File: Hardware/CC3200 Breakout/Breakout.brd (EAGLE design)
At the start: 58.4 x 76.3 mm, 5 parts, among them P1 SSW-110-02-G-D, P2 SSW-110-02-G-D, X1 TSW-105-07-G-S

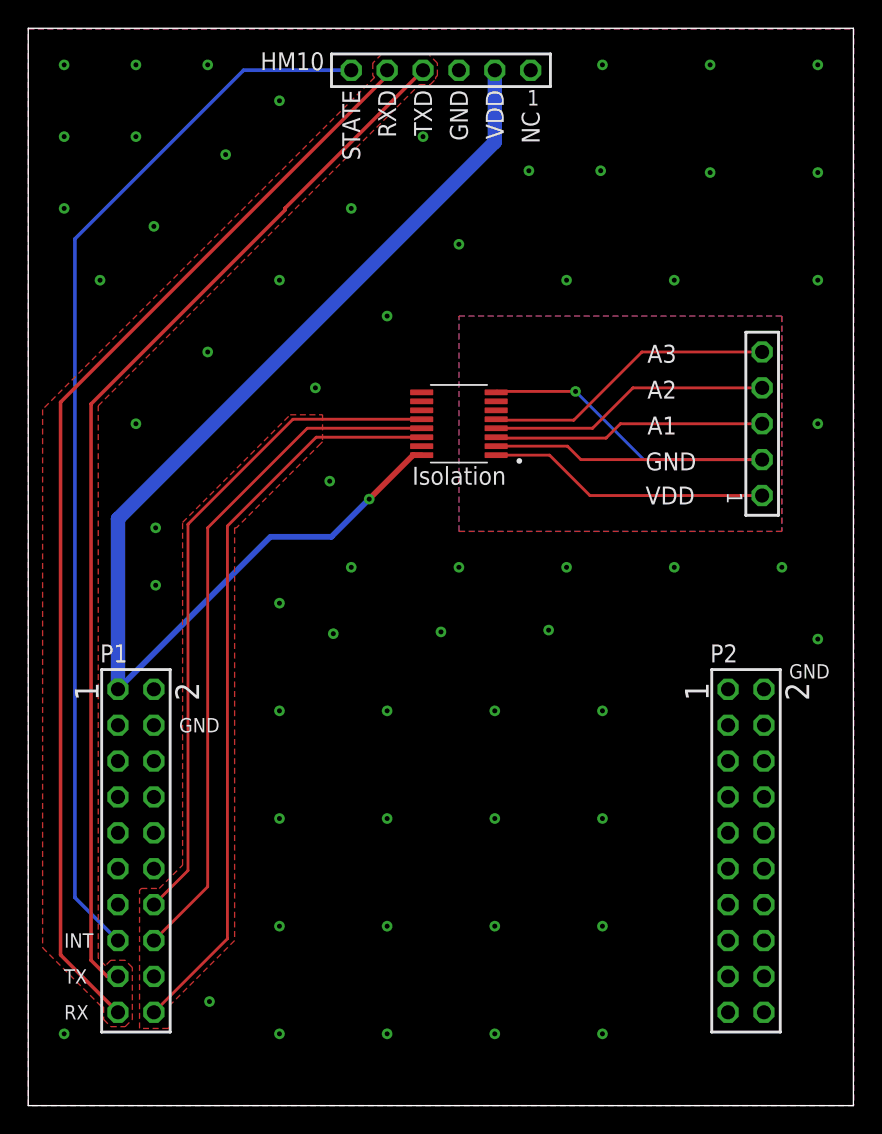
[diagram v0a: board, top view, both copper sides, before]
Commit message: Updated the breakout schematics
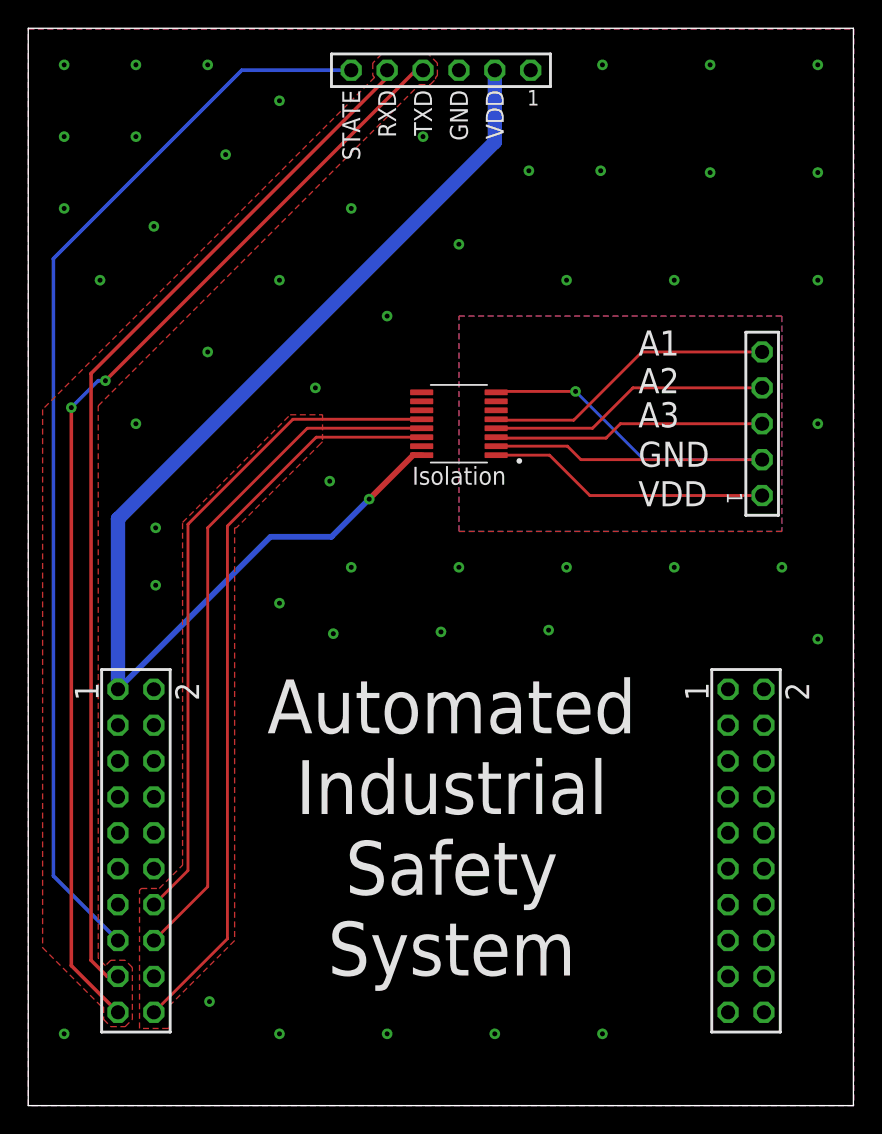
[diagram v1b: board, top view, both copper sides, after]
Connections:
- removed net RX: HM10.5, P1.19
- removed net TX: HM10.4, P1.17
- new net 3200_RX: HM10.4, P1.19
- new net 3200_TX: HM10.5, P1.17
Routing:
- net 3200_RX: track 0.00 -> 78.9 mm, vias 0 -> 2
- net RX: track 77.9 -> 0.00 mm
- net TX: track 75.1 -> 0.00 mm
- net 3200_TX: track 0.00 -> 74.1 mm
- net STATE: track 75.4 -> 76.8 mm
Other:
- board text added: "Automated Industrial Safety System"
- board text removed: "INT"
- board text removed: "NC"
- board text removed: "RX"
- board text removed: "TX"
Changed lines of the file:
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@@
 <layer number="24" name="bOrigins" color="15" fill="1" visible="yes" active="yes"/>
 <layer number="25" name="tNames" color="7" fill="1" visible="yes" active="yes"/>
-<layer number="26" name="bNames" color="7" fill="1" visible="yes" active="yes"/>
-<layer number="27" name="tValues" color="7" fill="1" visible="yes" active="yes"/>
-<layer number="28" name="bValues" color="7" fill="1" visible="yes" active="yes"/>
+<layer number="26" name="bNames" color="7" fill="1" visible="no" active="yes"/>
+<layer number="27" name="tValues" color="7" fill="1" visible="no" active="yes"/>
+<layer number="28" name="bValues" color="7" fill="1" visible="no" active="yes"/>
 <layer number="29" name="tStop" color="7" fill="3" visible="no" active="yes"/>
 <layer number="30" name="bStop" color="7" fill="6" visible="no" active="yes"/>
@@
 <dimension x1="6.35" y1="6.604" x2="6.35" y2="0" x3="-10.16" y3="3.302" textsize="1.778" layer="47" unit="mil" precision="3"/>
 <dimension x1="35.56" y1="73.279" x2="35.56" y2="76.2" x3="63.5" y3="74.7395" textsize="1.778" layer="47" unit="mil" precision="3"/>
-<text x="2.54" y="6.096" size="1.016" layer="25">RX</text>
-<text x="2.54" y="8.636" size="1.016" layer="25">TX</text>
-<text x="2.54" y="11.176" size="1.016" layer="25">INT</text>
-<text x="10.668" y="26.416" size="1.016" layer="25">GND</text>
-<text x="32.385" y="71.882" size="1.27" layer="25" rot="R270">VDD</text>
-<text x="29.845" y="71.882" size="1.27" layer="25" rot="R270">GND</text>
-<text x="27.305" y="71.882" size="1.27" layer="25" rot="R270">TXD</text>
-<text x="24.765" y="71.882" size="1.27" layer="25" rot="R270">RXD</text>
-<text x="22.225" y="71.882" size="1.27" layer="25" rot="R270">STATE</text>
-<text x="34.925" y="70.358" size="1.27" layer="25" rot="R270">NC</text>
-<text x="43.688" y="42.545" size="1.27" layer="25">VDD</text>
-<text x="43.688" y="44.958" size="1.27" layer="25">GND</text>
-<text x="43.815" y="47.498" size="1.27" layer="25">A1</text>
-<text x="43.815" y="50.038" size="1.27" layer="25">A2</text>
-<text x="43.815" y="52.578" size="1.27" layer="25">A3</text>
-<text x="27.178" y="43.942" size="1.27" layer="25">Isolation</text>
-<text x="53.848" y="30.226" size="1.016" layer="25">GND</text>
+<text x="32.385" y="71.882" size="1.27" layer="21" rot="R270">VDD</text>
+<text x="29.845" y="71.882" size="1.27" layer="21" rot="R270">GND</text>
+<text x="27.305" y="71.882" size="1.27" layer="21" rot="R270">TXD</text>
+<text x="24.765" y="71.882" size="1.27" layer="21" rot="R270">RXD</text>
+<text x="22.225" y="71.882" size="1.27" layer="21" rot="R270">STATE</text>
+<text x="27.178" y="43.942" size="1.27" layer="21">Isolation</text>
+<text x="43.18" y="42.418" size="1.778" layer="21">VDD</text>
+<text x="43.18" y="45.212" size="1.778" layer="21">GND</text>
+<text x="43.18" y="48.006" size="1.778" layer="21">A3</text>
+<text x="43.18" y="50.419" size="1.778" layer="21">A2</text>
+<text x="43.18" y="53.086" size="1.778" layer="21">A1</text>
+<text x="29.972" y="19.685" size="3.81" layer="21" align="center">Automated
+Industrial
+Safety
+System</text>
 </plain>
 <attributes>
@@
 <attribute name="MF" value="Samtec Inc." x="52.07" y="35.179" size="1.778" layer="27" display="off"/>
 <attribute name="MPN" value="TSW-106-07-G-S" x="52.07" y="35.179" size="1.778" layer="27" display="off"/>
-<attribute name="NAME" x="20.955" y="74.549" size="1.27" layer="25" rot="R180"/>
 <attribute name="OC_FARNELL" value="" x="52.07" y="35.179" size="1.778" layer="27" display="off"/>
 <attribute name="OC_NEWARK" value="" x="52.07" y="35.179" size="1.778" layer="27" display="off"/>
@@
 <attribute name="MF" value="Samtec Inc." x="2.54" y="-9.906" size="1.778" layer="27" rot="R270" display="off"/>
 <attribute name="MPN" value="SSW-110-02-G-D" x="2.54" y="-9.906" size="1.778" layer="27" rot="R270" display="off"/>
-<attribute name="NAME" x="5.08" y="31.369" size="1.27" layer="25"/>
 <attribute name="OC_FARNELL" value="unknown" x="2.54" y="-9.906" size="1.778" layer="27" rot="R270" display="off"/>
 <attribute name="OC_NEWARK" value="11P9480" x="2.54" y="-9.906" size="1.778" layer="27" rot="R270" display="off"/>
@@
 <attribute name="MF" value="Samtec Inc." x="27.94" y="-9.906" size="1.778" layer="27" rot="R270" display="off"/>
 <attribute name="MPN" value="SSW-110-02-G-D" x="27.94" y="-9.906" size="1.778" layer="27" rot="R270" display="off"/>
-<attribute name="NAME" x="48.26" y="31.369" size="1.27" layer="25"/>
 <attribute name="OC_FARNELL" value="unknown" x="27.94" y="-9.906" size="1.778" layer="27" rot="R270" display="off"/>
 <attribute name="OC_NEWARK" value="11P9480" x="27.94" y="-9.906" size="1.778" layer="27" rot="R270" display="off"/>
@@
 <via x="22.86" y="38.1" extent="1-16" drill="0.35"/>
 <via x="17.78" y="35.56" extent="1-16" drill="0.35"/>
-<via x="17.78" y="27.94" extent="1-16" drill="0.35"/>
-<via x="17.78" y="20.32" extent="1-16" drill="0.35"/>
-<via x="17.78" y="12.7" extent="1-16" drill="0.35"/>
 <via x="12.827" y="7.366" extent="1-16" drill="0.35"/>
 <via x="2.54" y="5.08" extent="1-16" drill="0.35"/>
@@
 <via x="33.02" y="5.08" extent="1-16" drill="0.35"/>
 <via x="40.64" y="5.08" extent="1-16" drill="0.35"/>
-<via x="25.4" y="12.7" extent="1-16" drill="0.35"/>
-<via x="40.64" y="12.7" extent="1-16" drill="0.35"/>
-<via x="33.02" y="12.7" extent="1-16" drill="0.35"/>
-<via x="40.64" y="20.32" extent="1-16" drill="0.35"/>
-<via x="33.02" y="20.32" extent="1-16" drill="0.35"/>
-<via x="25.4" y="20.32" extent="1-16" drill="0.35"/>
-<via x="40.64" y="27.94" extent="1-16" drill="0.35"/>
-<via x="33.02" y="27.94" extent="1-16" drill="0.35"/>
-<via x="25.4" y="27.94" extent="1-16" drill="0.35"/>
 <via x="36.83" y="33.655" extent="1-16" drill="0.35"/>
 <via x="29.21" y="33.528" extent="1-16" drill="0.35"/>
@@
 <via x="55.88" y="66.04" extent="1-16" drill="0.35"/>
 </signal>
-<signal name="TX">
-<contactref element="HM10" pad="4"/>
-<contactref element="P1" pad="17"/>
-<wire x1="6.35" y1="9.144" x2="5.588" y2="9.144" width="0.254" layer="1"/>
-<wire x1="5.588" y1="9.144" x2="4.445" y2="10.287" width="0.254" layer="1"/>
-<wire x1="4.445" y1="10.287" x2="4.445" y2="49.657" width="0.254" layer="1"/>
-<wire x1="18.161" y1="63.5" x2="18.161" y2="63.373" width="0.254" layer="1"/>
-<wire x1="18.161" y1="63.5" x2="27.94" y2="73.279" width="0.254" layer="1"/>
-<wire x1="4.445" y1="49.657" x2="18.161" y2="63.373" width="0.254" layer="1"/>
-</signal>
-<signal name="RX">
-<contactref element="HM10" pad="5"/>
-<contactref element="P1" pad="19"/>
-<wire x1="25.4" y1="73.279" x2="25.4" y2="72.898" width="0.254" layer="1"/>
-<wire x1="25.4" y1="72.898" x2="2.286" y2="49.784" width="0.254" layer="1"/>
-<wire x1="2.286" y1="49.784" x2="2.286" y2="10.668" width="0.254" layer="1"/>
-<wire x1="2.286" y1="10.668" x2="6.35" y2="6.604" width="0.254" layer="1"/>
-</signal>
 <signal name="STATE">
 <contactref element="HM10" pad="6"/>
 <contactref element="P1" pad="15"/>
-<wire x1="6.35" y1="11.684" x2="3.302" y2="14.732" width="0.254" layer="16"/>
-<wire x1="3.302" y1="14.732" x2="3.302" y2="61.341" width="0.254" layer="16"/>
-<wire x1="22.86" y1="73.279" x2="15.24" y2="73.279" width="0.254" layer="16"/>
-<wire x1="15.24" y1="73.279" x2="3.302" y2="61.341" width="0.254" layer="16"/>
+<wire x1="6.35" y1="11.684" x2="1.778" y2="16.256" width="0.254" layer="16"/>
+<wire x1="1.778" y1="16.256" x2="1.778" y2="59.944" width="0.254" layer="16"/>
+<wire x1="22.86" y1="73.279" x2="15.113" y2="73.279" width="0.254" layer="16"/>
+<wire x1="15.113" y1="73.279" x2="1.778" y2="59.944" width="0.254" layer="16"/>
 </signal>
 <signal name="VBUS">
@@
 </polygon>
 </signal>
+<signal name="3200_RX">
+<contactref element="HM10" pad="4"/>
+<contactref element="P1" pad="19"/>
+<wire x1="6.35" y1="6.604" x2="3.048" y2="9.906" width="0.254" layer="1"/>
+<via x="3.048" y="49.403" extent="1-16" drill="0.35"/>
+<wire x1="3.048" y1="9.906" x2="3.048" y2="49.403" width="0.254" layer="1"/>
+<wire x1="3.048" y1="49.403" x2="4.953" y2="51.308" width="0.254" layer="16"/>
+<wire x1="4.953" y1="51.308" x2="5.461" y2="51.308" width="0.254" layer="16"/>
+<via x="5.461" y="51.308" extent="1-16" drill="0.35"/>
+<wire x1="5.461" y1="51.308" x2="27.432" y2="73.279" width="0.254" layer="1"/>
+<wire x1="27.432" y1="73.279" x2="27.94" y2="73.279" width="0.254" layer="1"/>
+</signal>
+<signal name="3200_TX">
+<contactref element="HM10" pad="5"/>
+<contactref element="P1" pad="17"/>
+<wire x1="6.35" y1="9.144" x2="5.588" y2="9.144" width="0.254" layer="1"/>
+<wire x1="5.588" y1="9.144" x2="4.445" y2="10.287" width="0.254" layer="1"/>
+<wire x1="25.4" y1="72.771" x2="25.4" y2="73.279" width="0.254" layer="1"/>
+<wire x1="4.445" y1="10.287" x2="4.445" y2="51.816" width="0.254" layer="1"/>
+<wire x1="4.445" y1="51.816" x2="25.4" y2="72.771" width="0.254" layer="1"/>
+</signal>
 </signals>
 <mfgpreviewcolors>
@@
 </drawing>
 <compatibility>
+<note version="6.3" minversion="6.2.2" severity="warning">
+Since Version 6.2.2 text objects can contain more than one line,
+which will not be processed correctly with this version.
+</note>
 <note version="8.2" severity="warning">
 Since Version 8.2, EAGLE supports online libraries. The ids
